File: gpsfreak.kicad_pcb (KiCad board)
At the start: 4 copper layers, 79.8 x 47.2 mm, 157 parts, among them J10 Skedd, J13 Boot, J2 SMA, J3 SMA, J4 SMA, J5 U.Fl, J6 SMA, J7 USB_C_Receptacle_16P, J8 U.Fl, J9 U.Fl, Q1 AO3400A, Q2 AO3401A, T2 MABA-010247-2R1250, U1 MAX-M10S, U11 74LVC1G07, U2 LMK05318BRGZR, U21 TMP117xxDRV, U3 TG5032CGN, U31 TLV3601DCKR, U32 TLV3601DCKR, U4 STM32H503KBUx, U5 TPS82084SIL, U6 TPS82084SIL, U7 TPS7A8801RTJR

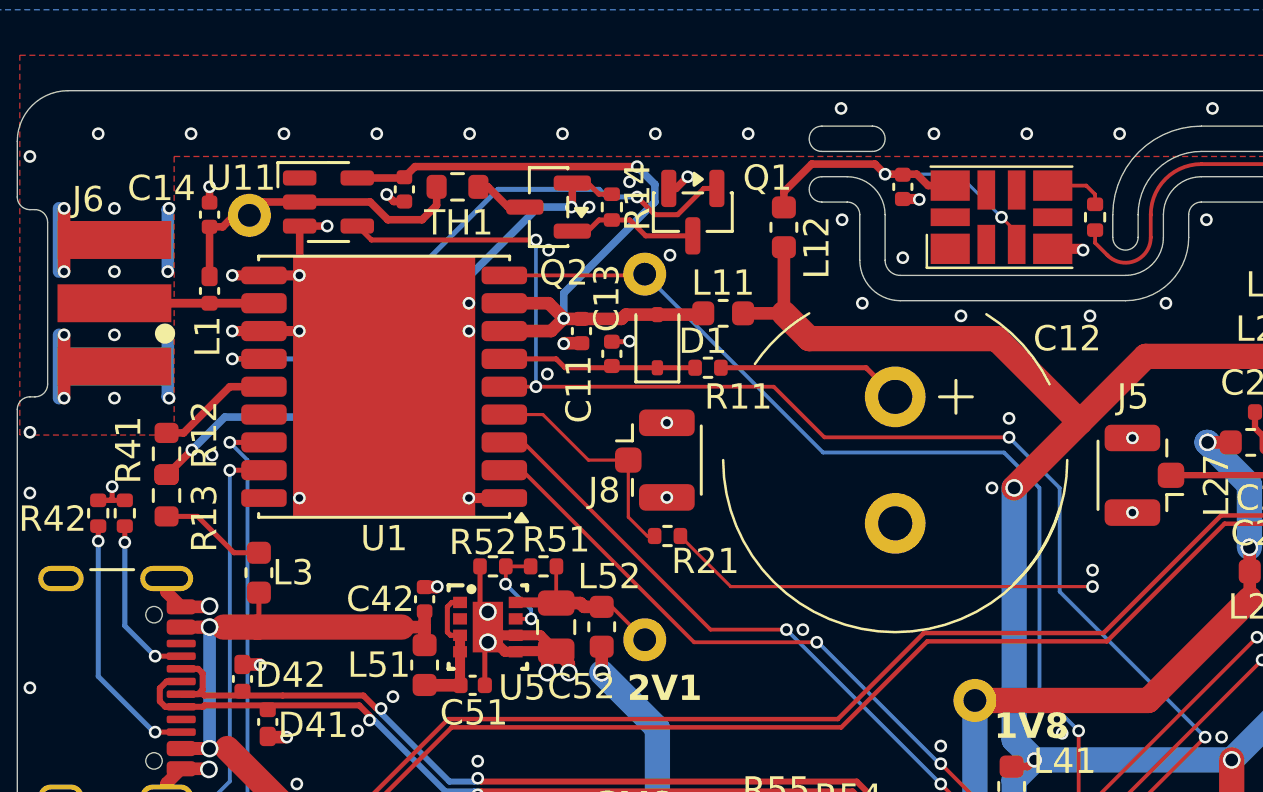
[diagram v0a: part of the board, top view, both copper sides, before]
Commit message: Remove unused components around GPS power.
(Ant. power switch & monitor, backup supercap.)
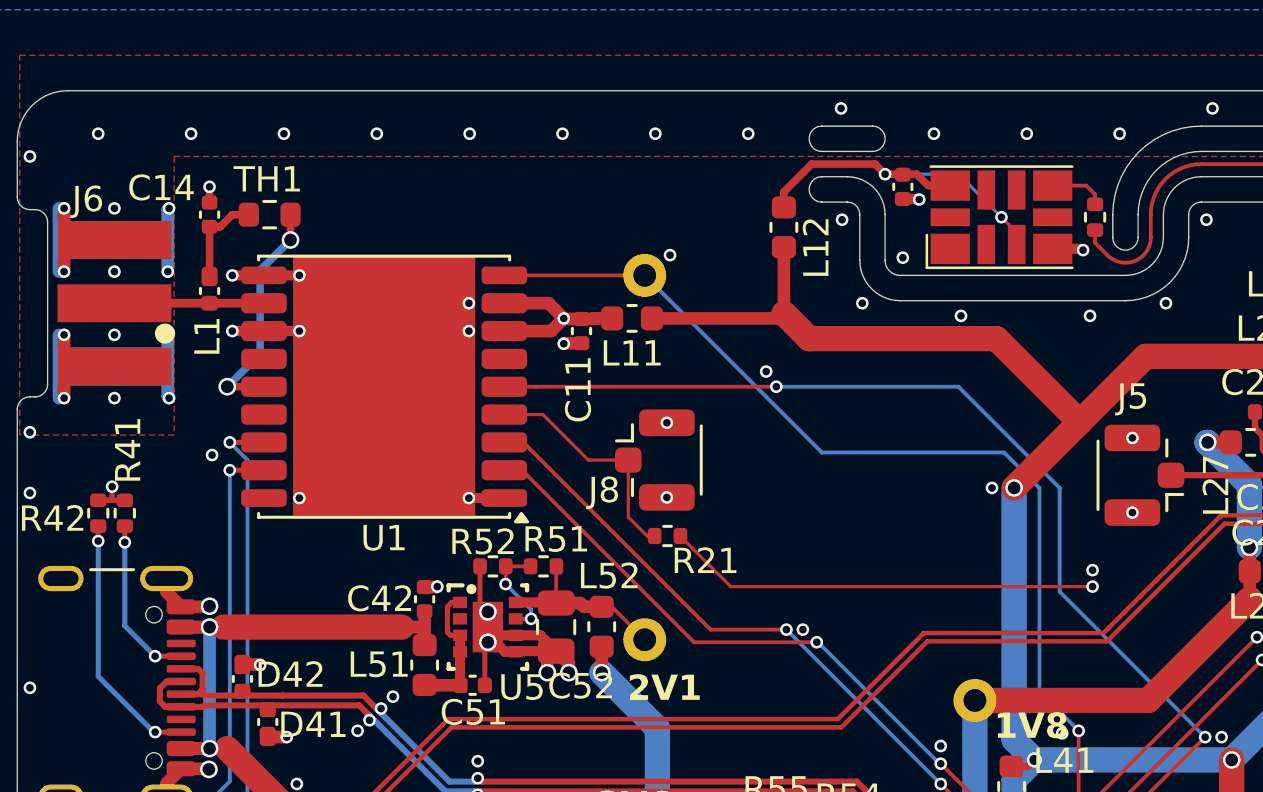
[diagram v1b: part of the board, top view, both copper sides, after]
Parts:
- removed C12: .47F, Parts:CP_Radial_D13.5mm_P5.00mm
- removed C13, C15: 0u1, Capacitor_SMD:C_0402_1005Metric
- removed D1: 1N4148WS, Diode_SMD:D_SOD-323
- removed L3: 220, Inductor_SMD:L_0603_1608Metric
- removed Q1: AO3400A, Package_TO_SOT_SMD:SOT-23
- removed Q2: AO3401A, Package_TO_SOT_SMD:SOT-23
- removed R11: 100, Resistor_SMD:R_0402_1005Metric
- removed R12, R13: 0, Resistor_SMD:R_0603_1608Metric
- removed R14: 100k, Resistor_SMD:R_0402_1005Metric
- removed TP2: TestPoint_Probe, Parts:TestPoint
- removed U11: 74LVC1G07, Parts:SOT-23-5
- moved TH1 7.51 mm to (108.8, 81.3)
- moved L11 3.61 mm to (123.1, 85.4)
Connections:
- net /GPS/VrfSW renamed Net-(C14-Pad1)
- TH1 pad 2: Net-(Q2-D) -> /GPS/VCC_RF
- U1 pad 13: /GPS/LNA_EN -> unconnected-(U1-LNA_EN-Pad13)
- U1 pad 6: /GPS/VBCKP -> unconnected-(U1-V_BCKP-Pad6)
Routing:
- net /GPS/LNA_EN: track 24.0 -> 0.00 mm, vias 2 -> 0
- net /GPS/VGPS: track 29.8 -> 7.08 mm, vias 2 -> 1
- net /GPS/Vrf: track 22.4 -> 0.00 mm, vias 2 -> 0
- net EXTINT: track 55.5 -> 42.4 mm, vias 4 -> 2
- net Net-(C14-Pad1): track 12.0 -> 3.71 mm
- net /GPS/VBCKP: track 7.68 -> 0.00 mm
- net Net-(C12-Pad1): track 7.37 -> 0.00 mm
- net GND: track 206.3 -> 200.8 mm, vias 300 -> 292
- net /GPS/VCC_RF: track 4.61 -> 9.29 mm, vias 0 -> 2
- net Net-(Q1-D): track 4.59 -> 0.00 mm
- net Net-(L3-Pad2): track 4.25 -> 0.00 mm
- net +3V3: track 176.2 -> 179.8 mm
- net Net-(Q2-D): track 2.17 -> 0.00 mm
- net VBus: track 33.1 -> 31.7 mm

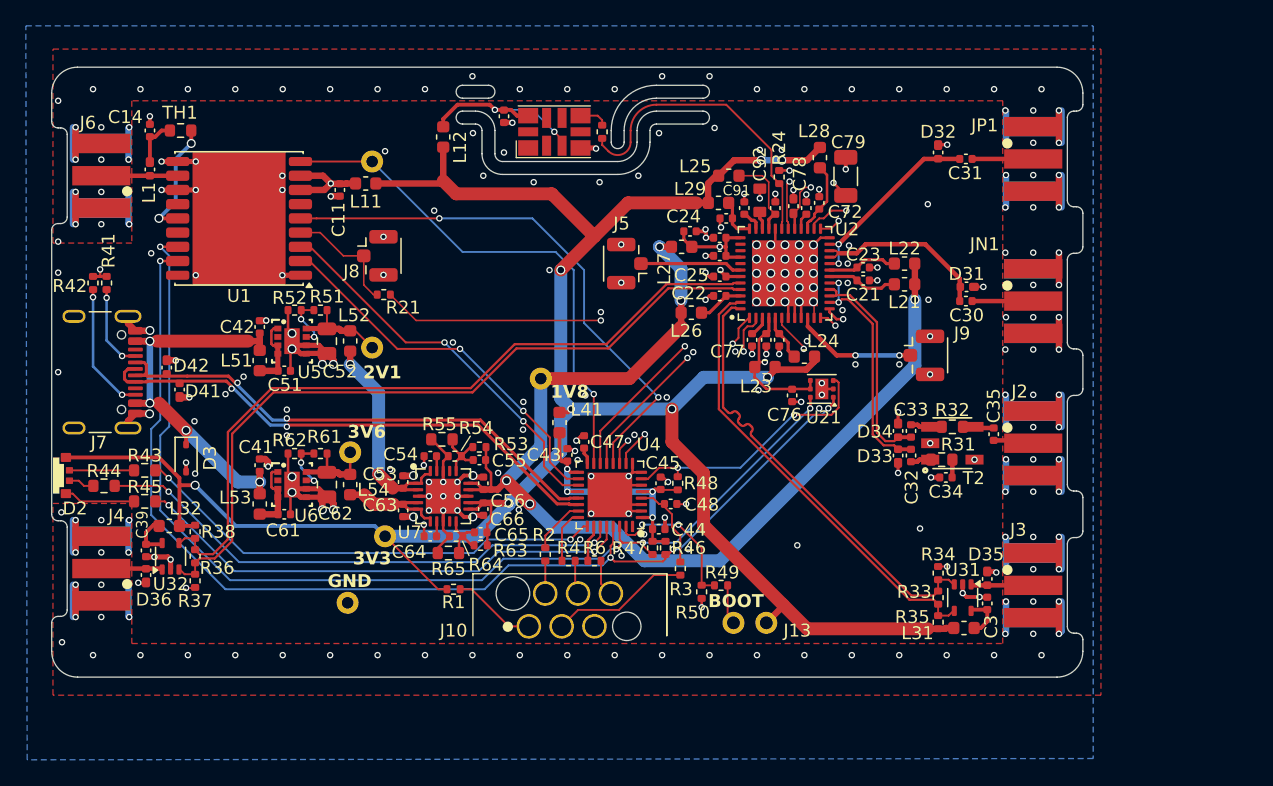
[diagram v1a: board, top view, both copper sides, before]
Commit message: FPGA in, layout mostly updated.
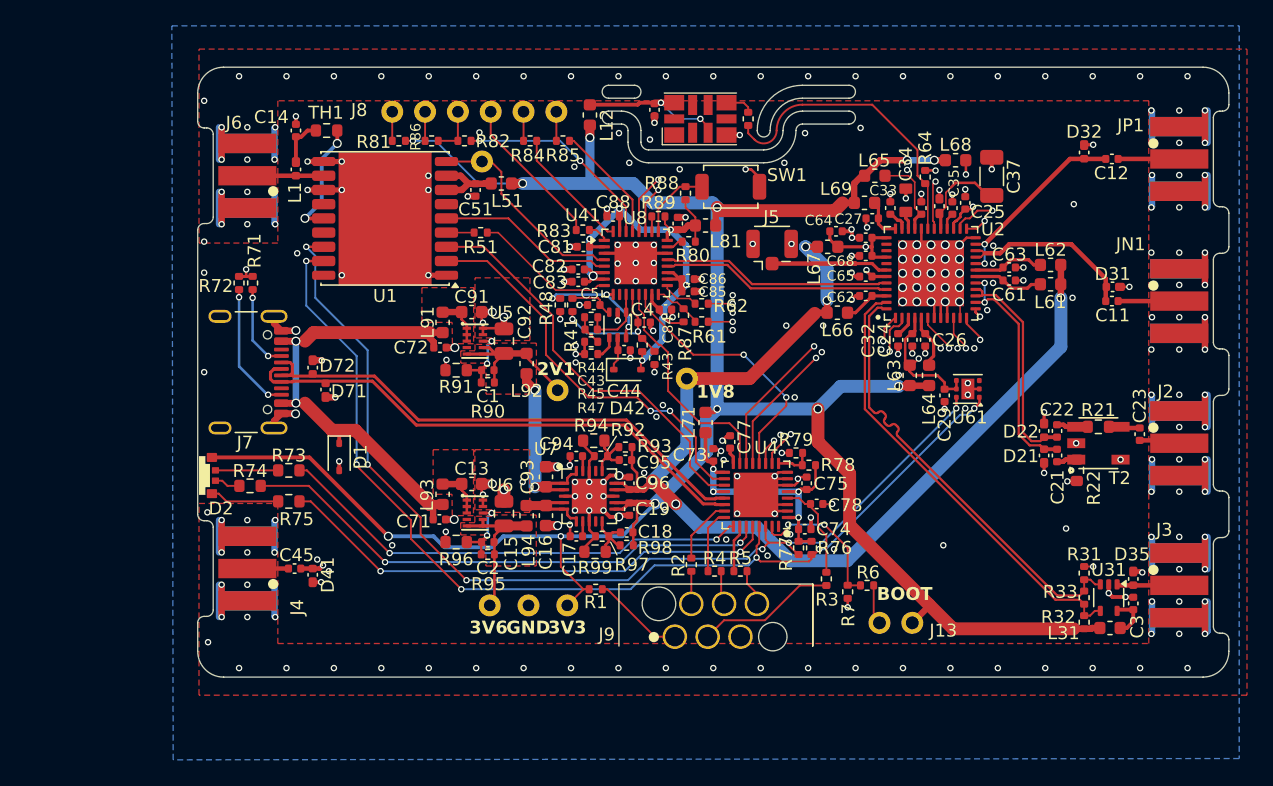
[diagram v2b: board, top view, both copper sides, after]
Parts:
- removed the C34 at (168.0, 108.2)
- removed C39: 10u, Capacitor_SMD:C_0402_1005Metric
- removed D36: D_TVS, Parts:HHS_0402
- removed the J9 at (166.3, 98.7)
- removed L32: 220, Inductor_SMD:L_0603_1608Metric
- removed R36: 100, Resistor_SMD:R_0402_1005Metric
- removed R37, R38: 100k, Resistor_SMD:R_0402_1005Metric
- removed U32: TLV3601DCKR, Parts:SOT-353_SC-70-5
- added C1: 470p, Capacitor_SMD:C_0402_1005Metric, F.Cu at (132.6, 99.8)
- added C2: 470p, Capacitor_SMD:C_0402_1005Metric, F.Cu at (132.6, 113.2)
- added C4: 10n, Capacitor_SMD:C_0402_1005Metric, F.Cu at (144.7, 96.2)
- added C43: 10p, Capacitor_SMD:C_0402_1005Metric, F.Cu at (140.6, 96.7)
- added C44: 0u1, Capacitor_SMD:C_0402_1005Metric, F.Cu at (143.1, 98.3)
- added C45: 0u1, Capacitor_SMD:C_0402_1005Metric, F.Cu at (117.6, 115.2)
- added C5: 0u1, Capacitor_SMD:C_0402_1005Metric, F.Cu at (140.8, 94.8)
- added C81: 1u, Capacitor_SMD:C_0402_1005Metric, F.Cu at (139.9, 90.3)
- added C82: 1u, Capacitor_SMD:C_0402_1005Metric, F.Cu at (139.6, 92.0)
- added C83: 1u, Capacitor_SMD:C_0402_1005Metric, F.Cu at (139.6, 93.0)
- added C84: 1u, Capacitor_SMD:C_0402_1005Metric, F.Cu at (146.3, 95.2)
- added C85: 1u, Capacitor_SMD:C_0402_1005Metric, F.Cu at (148.1, 93.8)
- added C86: 1u, Capacitor_SMD:C_0402_1005Metric, F.Cu at (148.1, 92.8)
- added C87: 1u, Capacitor_SMD:C_0402_1005Metric, F.Cu at (147.2, 88.5)
- added C88: 1u, Capacitor_SMD:C_0402_1005Metric, F.Cu at (142.2, 88.0)
- added D41: D_TVS, Parts:HHS_0402, F.Cu at (119.0, 115.7)
- added D42: 1N5819WS, Diode_SMD:D_SOD-323, F.Cu at (143.3, 99.8)
- added L81: 220, Inductor_SMD:L_0603_1608Metric, F.Cu at (149.4, 88.7)
- added R41: 10k, Resistor_SMD:R_0402_1005Metric, F.Cu at (139.1, 94.8)
- added R42: 10k, Resistor_SMD:R_0402_1005Metric, F.Cu at (144.5, 97.9)
- added R43: 10k, Resistor_SMD:R_0402_1005Metric, F.Cu at (145.4, 98.9)
- added R44: 1k, Resistor_SMD:R_0402_1005Metric, F.Cu at (140.6, 95.8)
- added R45: 100, Resistor_SMD:R_0402_1005Metric, F.Cu at (140.6, 97.7)
- added R47: 39, Resistor_SMD:R_0402_1005Metric, F.Cu at (140.6, 98.6)
- added R51: 100, Resistor_SMD:R_0402_1005Metric, F.Cu at (132.0, 89.2)
- added R62: 100, Resistor_SMD:R_0402_1005Metric, F.Cu at (149.1, 94.7)
- added R78: 10k, Resistor_SMD:R_0402_1005Metric, F.Cu at (157.4, 107.2)
- added R79: 10k, Resistor_SMD:R_0402_1005Metric, F.Cu at (156.4, 106.2)
- added R80: 5k1, Resistor_SMD:R_0402_1005Metric, F.Cu at (148.1, 89.9)
- added R81: 100, Resistor_SMD:R_0402_1005Metric, F.Cu at (125.7, 82.1)
- added R82: 100, Resistor_SMD:R_0402_1005Metric, F.Cu at (130.7, 82.1)
- added R83: 100, Resistor_SMD:R_0402_1005Metric, F.Cu at (139.9, 89.0)
- added R84: 100, Resistor_SMD:R_0402_1005Metric, F.Cu at (135.8, 82.1)
- added R85: 100, Resistor_SMD:R_0402_1005Metric, F.Cu at (138.4, 82.1)
- added R86: 5k1, Resistor_SMD:R_0402_1005Metric, F.Cu at (128.2, 82.1)
- added R87: 5k1, Resistor_SMD:R_0402_1005Metric, F.Cu at (147.7, 95.6)
- added R88: 5k1, Resistor_SMD:R_0402_1005Metric, F.Cu at (147.8, 86.2)
- added R89: 5k1, Resistor_SMD:R_0402_1005Metric, F.Cu at (145.8, 88.0)
- added SW1: SW_Push, Button_Switch_SMD:SW_SPST_TS-1088-xR020, F.Cu at (151.3, 85.7)
- added U41: TS5A63157DBV, Parts:SOT-353_SC-70-6, F.Cu at (142.6, 96.3)
- added U8: LCMXO2-256HC-4SG32C, Package_DFN_QFN:QFN-32-1EP_5x5mm_P0.5mm_EP3.3x3.3mm, F.Cu at (144.0, 91.5)
- C13: renamed from C61; footprint Capacitor_SMD:C_0402_1005Metric -> Capacitor_SMD:C_0603_1608Metric
- C16: renamed from C63; footprint Capacitor_SMD:C_0402_1005Metric -> Capacitor_SMD:C_0603_1608Metric
- C91: renamed from C51; footprint Capacitor_SMD:C_0402_1005Metric -> Capacitor_SMD:C_0603_1608Metric
- C93: renamed from C53; footprint Capacitor_SMD:C_0402_1005Metric -> Capacitor_SMD:C_0603_1608Metric
- J8: value U.Fl -> Conn_01x06; footprint Parts:U.FL_Hirose_U.FL-R-SMT-1_Vertical -> Parts:PinHeader_1x06_P2.54mm_Vertical
- R90: renamed from R51; value 39k -> 75k
- R91: renamed from R52; value 24k -> 30k; footprint Resistor_SMD:R_0402_1005Metric -> Resistor_SMD:R_0603_1608Metric
- R95: renamed from R61; value 200k -> 150k
- R96: renamed from R62; value 56k -> 30k; footprint Resistor_SMD:R_0402_1005Metric -> Resistor_SMD:R_0603_1608Metric
- TP4: value TestPoint_Probe -> 2V2
- U5, U6: value TPS82084SIL -> TPSM82822SILR; footprint Parts:SIL0008C_SMD_NV -> Parts:SIL0010D-MFG
- moved R61 24.7 mm to (149.1, 96.1)
- moved J8 17.8 mm to (137.9, 79.8), turned to -90 degrees
- moved R48 16.5 mm to (138.2, 94.8), turned to 90 degrees
- moved TP5 16.0 mm to (132.7, 118.0)
- moved C91 15.2 mm to (131.3, 95.3)
- moved R95 15.1 mm to (132.6, 114.1)
- moved TP7 15.1 mm to (138.7, 118.0)
- moved TP4 14.7 mm to (137.9, 101.4)
- moved C13 14.7 mm to (131.3, 108.7)
- moved C71 14.5 mm to (128.8, 111.4), turned to 180 degrees
- moved L91 14.5 mm to (129.1, 96.2), turned to 90 degrees
- moved U6 14.3 mm to (131.6, 110.9)
- moved R96 14.3 mm to (130.1, 113.2)
- moved L93 14.2 mm to (129.1, 109.5), turned to 90 degrees
- moved U5 14.2 mm to (131.6, 97.6)
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- renumbered C30 to C11, C31 to C12, C62 to C15, C64 to C17, C65 to C18, C66 to C19, C32 to C21, C33 to C22, C35 to C23, C71 to C24, C72 to C25, C73 to C26, C74 to C27, C75 to C28, C76 to C29, C29 to C31, C77 to C32, C91 to C33, C92 to C34, C93 to C35, C78 to C36, C79 to C37, C11 to C51, C21 to C61, C22 to C62, C23 to C63, C24 to C64, C25 to C65, C27 to C67, C28 to C68, C41 to C71, C42 to C72, C43 to C73, C44 to C74, C45 to C75, C47 to C77, C48 to C78, C52 to C92, C54 to C94, C55 to C95, C56 to C96, D3 to D1, D33 to D21, D34 to D22, D41 to D71, D42 to D72, J10 to J9, L11 to L51, L21 to L61, L22 to L62, L23 to L63, L24 to L64, L25 to L65, L26 to L66, L27 to L67, L28 to L68, L29 to L69, L41 to L71, L51 to L91, L52 to L92, L53 to L93, L54 to L94, R32 to R21, R31 to R22, R34 to R31, R35 to R32, R6 to R5, R49 to R6, R21 to R61, R23 to R63, R24 to R64, R50 to R7, R41 to R71, R42 to R72, R43 to R73, R44 to R74, R45 to R75, R46 to R76, R47 to R77, R54 to R92, R53 to R93, R55 to R94, R64 to R97, R63 to R98, R65 to R99, U21 to U61
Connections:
- net /Clocking/GPSCLKLO renamed /Clocking/PRIREFLO
- J4 pad 1: /Output4/Ext3 -> Net-(J4-In)
- J8 pad 1: GPSCLK -> /FPGA/dTMS
- J8 pad 2: GND -> /FPGA/dTDI
- R22 pad 1: Net-(C34-Pad2) -> GND
- R48 pad 1: ALERT -> GND
- R48 pad 2: /CPU/VCPU -> /FPGA/ClkOEN
- R61 pad 1: GPSCLK -> PRIREF
- U1 pad 4: GPSCLK -> Net-(U1-TIMEPULSE)
- U2 pad 10: /Clocking/SecRef -> /Clocking/SECREFLO
- U4 pad 12: EXTINT -> EXTINTF
- U4 pad 15: GPS_nRST -> GPS_nRSTF
- U4 pad 7: ALERT -> GND
- U4 pad 9: GND -> /CPU/HWID
- U5 pad 2: unconnected-(U5-PG-Pad2) -> /Power/In2V1
- U5 pad 4: /Power/In2V1 -> unconnected-(U5-PG-Pad4)
- U5 pad 5: GND -> /Power/2V1
- U5 pad 6: GND -> /Power/2V1
- U5 pad 7: /Power/Fb21 -> /Power/2V1
- U5 pad 8: /Power/2V1 -> /Power/Fb21
- U6 pad 2: unconnected-(U6-PG-Pad2) -> /Power/In3V6
- U6 pad 4: /Power/In3V6 -> unconnected-(U6-PG-Pad4)
- U6 pad 5: GND -> /Power/3V6
- U6 pad 6: GND -> /Power/3V6
- U6 pad 7: /Power/Fb36 -> /Power/3V6
- U6 pad 8: /Power/3V6 -> /Power/Fb36
- U61 pad 3: ALERT -> unconnected-(U61-ALERT-Pad3)
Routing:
- net /FPGA/VFPGA: track 0.00 -> 46.2 mm, vias 0 -> 7
- net /OUT4_N: track 58.2 -> 17.8 mm
- net /OUT4_P: track 58.2 -> 17.8 mm
- net I2C_SCL: track 106.3 -> 136.9 mm, vias 5 -> 8
- net I2C_SDA: track 102.7 -> 132.5 mm, vias 5 -> 8
- net /Output4/IO: track 0.00 -> 29.8 mm, vias 0 -> 2
- net EXTINT: track 42.4 -> 13.7 mm, vias 2 -> 0
- net /Clocking/SECREFLO: track 0.00 -> 24.1 mm, vias 0 -> 2
- net GPS_nRST: track 40.2 -> 16.4 mm, vias 1 -> 0
- net EXTINTF: track 0.00 -> 20.7 mm, vias 0 -> 2
- net ALERT: track 20.4 -> 0.00 mm, vias 2 -> 0
- net GPS_nRSTF: track 0.00 -> 17.7 mm
- net /FPGA/TCK: track 0.00 -> 16.0 mm, vias 0 -> 2
- net /Clocking/PRIREFLO: track 36.8 -> 22.5 mm
- net /FPGA/dTDO: track 0.00 -> 11.9 mm
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- added copper zone on F.Cu, net /Power/2V1
- added copper zone on F.Cu, net /Power/3V6
- added copper zone on F.Cu, net /Power/In2V1
- added copper zone on F.Cu, net /Power/In3V6
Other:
- outline, holes or cut-outs redrawn

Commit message: Layout down
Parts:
- removed the C36 at (167.5, 87.2)
- removed D71, D72: D_TVS, Parts:HHS_0402
- added C19: 22u, Capacitor_SMD:C_0603_1608Metric, F.Cu at (145.0, 111.8)
- added C73: 1u, Capacitor_SMD:C_0402_1005Metric, F.Cu at (120.0, 99.0)
- added C97: 22u, Capacitor_SMD:C_0603_1608Metric, F.Cu at (146.5, 111.8)
- added U71: USBLC6-2SC6, Parts:SOT-666-6, F.Cu at (120.0, 100.5)
- C65, C67, C68: value 0u1 -> 1u
- C81, C85: value 1u -> 10u
- L1: value 100n -> 68n
- L12, L31, L51, L61, L62, L63, L64, L65, L66, L67, L68, L69, L71, L81, L91, L92, L93, L94: value 220 -> 120
- R22: value 50 -> 49.9
- R47: value 39 -> 33
- R94: footprint Resistor_SMD:R_0603_1608Metric -> Resistor_SMD:R_0402_1005Metric
- U41: footprint Parts:SOT-353_SC-70-6 -> Parts:SOT-363_SC-70-6
- U8: footprint Package_DFN_QFN:QFN-32-1EP_5x5mm_P0.5mm_EP3.3x3.3mm -> Parts:QFN-32-1EP_5x5mm_P0.5mm_EP3.5x3.5mm
- moved R43 7.10 mm to (138.7, 96.7), turned to 180 degrees
- moved C36 3.65 mm to (168.1, 83.8)
- moved L68 2.98 mm to (170.7, 85.9), turned to -90 degrees
- moved SW1 2.00 mm to (153.3, 85.7)
- moved R88 1.00 mm to (148.8, 86.2)
- moved C29 0.95 mm to (167.9, 100.8)
- moved U61 0.95 mm to (169.7, 100.3)
- moved R94 0.60 mm to (141.3, 105.5)
- moved R87 0.50 mm to (147.7, 96.1)
- moved C25 0.40 mm to (169.4, 87.3)
- moved TP4 0.38 mm to (137.8, 101.0)
- moved R62 0.30 mm to (148.8, 94.7)
- moved R64 0.15 mm to (166.4, 85.0)
- renumbered C18 to C17, C19 to C18, C17 to C20, C37 to C36, C84 to C6, C73 to C74, C74 to C75, C75 to C76
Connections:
- R61 pad 1: PRIREF -> Net-(U8-PB9A)
- R61 pad 2: /Clocking/PRIREFLO -> PRIREF
- R62 pad 1: SECREF -> Net-(U8-PB9B)
- R62 pad 2: /Clocking/SECREFLO -> SECREF
- R87 pad 2: PRIREF -> Net-(U8-PB9A)
- U2 pad 10: /Clocking/SECREFLO -> SECREF
- U2 pad 6: /Clocking/PRIREFLO -> PRIREF
- U8 pad 16: PRIREF -> Net-(U8-PB9A)
- U8 pad 17: SECREF -> Net-(U8-PB9B)
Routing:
- net /Clocking/SECREFLO: track 24.1 -> 0.00 mm, vias 2 -> 0
- net /Clocking/PRIREFLO: track 22.5 -> 0.00 mm, vias 2 -> 0
- net SECREF: track 2.87 -> 24.4 mm, vias 0 -> 2
- net PRIREF: track 3.79 -> 22.5 mm, vias 0 -> 2
- net I2C_SDA: track 132.5 -> 127.0 mm
- net I2C_SCL: track 136.9 -> 132.0 mm
- net VBus: track 38.1 -> 43.0 mm, vias 2 -> 4
- net +3V3: track 184.2 -> 188.9 mm
- net Net-(U8-PB9A): track 0.00 -> 4.01 mm
- net /Clocking/VDD_DIG: track 18.6 -> 14.7 mm, vias 2 -> 0
- net /Clocking/LF1: track 7.30 -> 3.81 mm
- net FINC: track 42.5 -> 39.2 mm
- net /Clocking/VDD_PLL1: track 6.44 -> 3.23 mm, vias 2 -> 0
- net Net-(U8-PB9B): track 0.00 -> 2.57 mm
- net /FPGA/PROGN: track 5.87 -> 7.70 mm
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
